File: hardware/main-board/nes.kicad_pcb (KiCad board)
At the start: 2 copper layers, 127 x 114.3 mm, 141 parts, among them J1 Power Jack, J2 Input Board, J3 Speaker, J4 Program, J5 NHD OLED Connector, J6 microSD Socket, Q1 SS8050, Q2 SS8050, Q3 SS8050, SW1 NES Reset, SW2 ESP Reset, U1 R-78E5.0-0.5, U10 74HCT00, U11 PCA9564, U12 MCP7940N, U13 ESP-WROOM-32, U15 EClamp2410P, U2 R-78E3.3-0.5, U3 74LVC1404, U4 RP2A03, U5 74HCT138, U6 LM4889, U7 AS6C6264, U8 MCP40D17, U9 AT28C64B, Y1 21.5 MHz, Y2 32.768 kHz

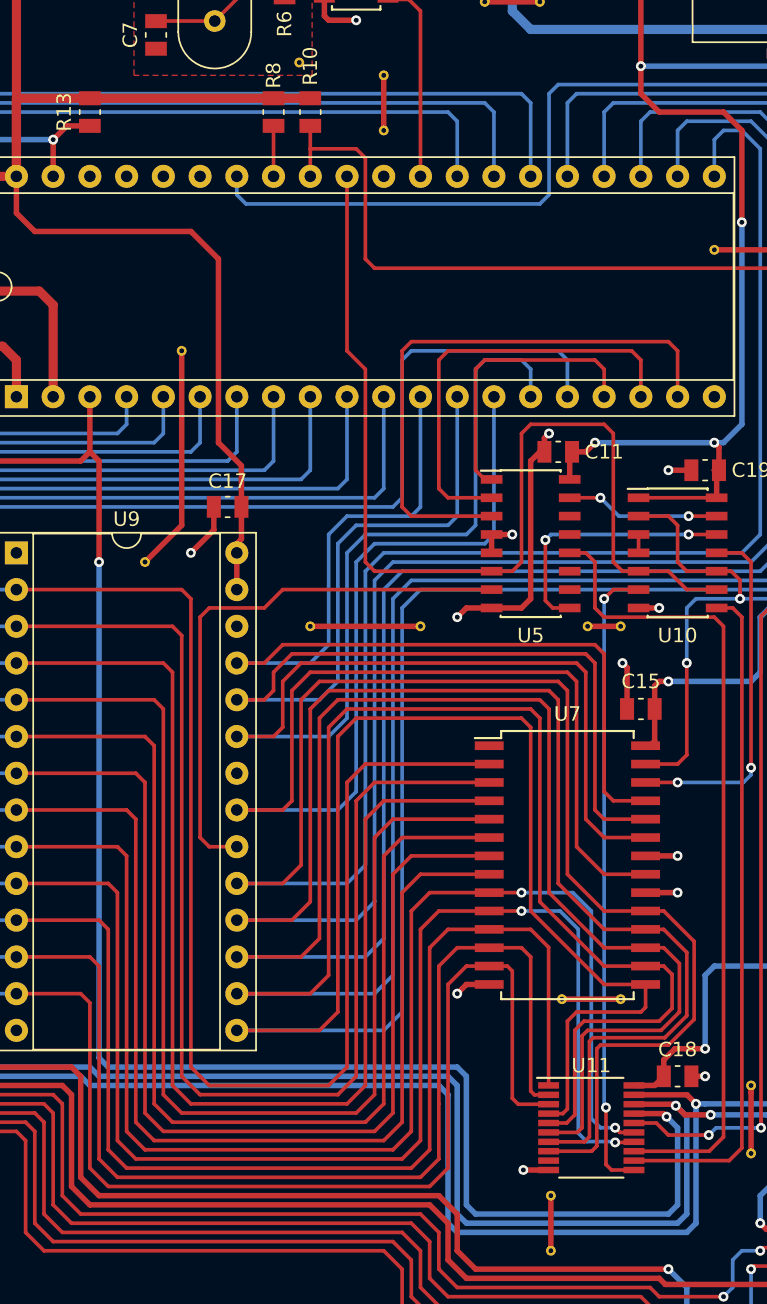
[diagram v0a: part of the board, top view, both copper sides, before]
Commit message: Route the OUT1 line from the RP2A03 to the PCA9564's reset pin
This change gives the NES CPU control over resetting its I2C controller,
for improved error recovery and more predictable startup behavior. Also
added a pull-up resistor, similar to how OUT0 was wired, for a more
predictable "high" voltage.

Fixes #8
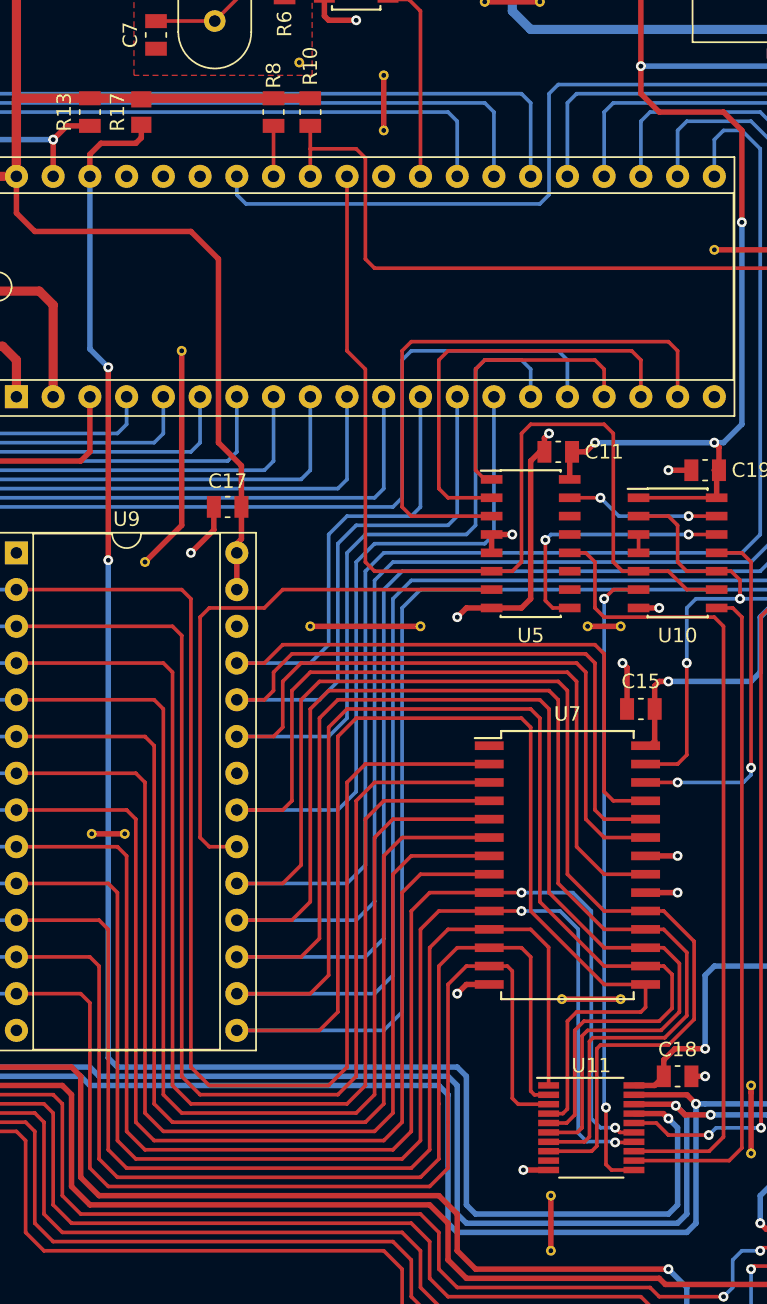
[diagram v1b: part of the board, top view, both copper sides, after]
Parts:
- added R17: 20k, Resistor_SMD:R_0805_2012Metric, F.Cu at (107.7, 49.5)
- added REF**: Via_27mill, lib_fp:Via_27mill, F.Cu at (104.3, 99.4)
- added REF**: Via_27mill, lib_fp:Via_27mill, F.Cu at (106.6, 99.4)
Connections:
- U11 pad 17: /NES CPU/~RST -> /NES CPU/OUT1
- U4 pad 38: Net-(U4-Pad38) -> /NES CPU/OUT1
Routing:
- net /NES CPU/OUT1: track 0.00 -> 126.5 mm, vias 0 -> 3
- net /NES CPU/~RST: track 122.0 -> 21.1 mm, vias 2 -> 0
- net GND: track 409.4 -> 411.7 mm

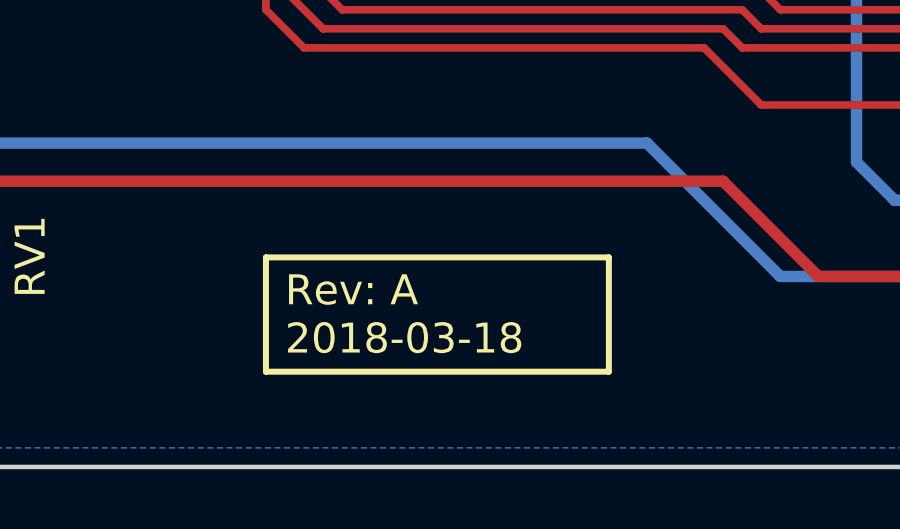
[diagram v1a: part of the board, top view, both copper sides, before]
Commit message: Updated schematic and PCB references for Rev B
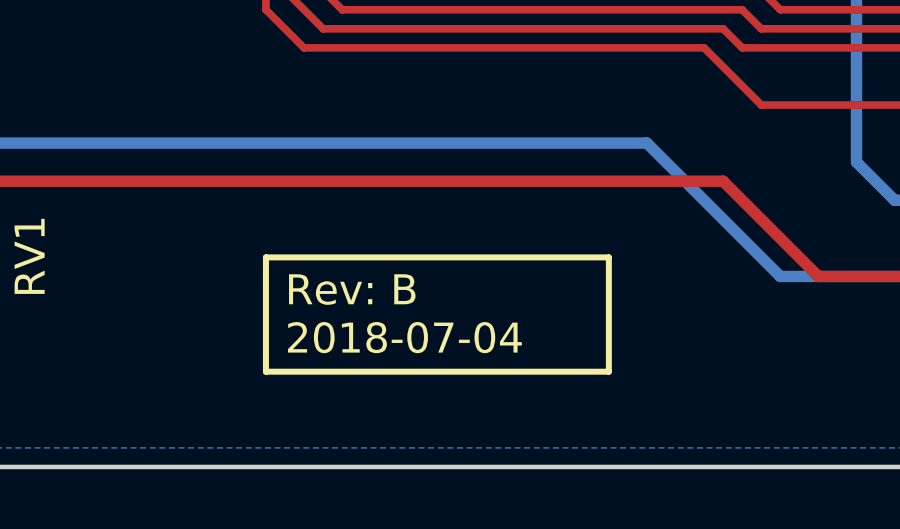
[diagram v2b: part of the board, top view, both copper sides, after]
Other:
- board text added: "Rev: B 2018-07-04"
- board text removed: "Rev: A 2018-03-18"
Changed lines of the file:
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@@
   (title_block
     (title "Nestronic Game Music Synthesizer")
-    (date 2018-03-13)
-    (rev A)
+    (date 2018-07-04)
+    (rev B)
     (company LogicProbe.org)
     (comment 1 "Derek Konigsberg")
@@
   )
   (setup
-    (last_trace_width 0.381)
+    (last_trace_width 0.1524)
     (user_trace_width 0.254)
     (user_trace_width 0.381)
@@
   (gr_line (start 125.73 144.145) (end 137.16 144.145) (angle 90) (layer F.SilkS) (width 0.2))
   (gr_line (start 125.73 140.335) (end 125.73 144.145) (angle 90) (layer F.SilkS) (width 0.2))
-  (gr_text "Rev: A\n2018-03-18" (at 126.365 142.24) (layer F.SilkS)
+  (gr_text "Rev: B\n2018-07-04" (at 126.365 142.24) (layer F.SilkS)
     (effects (font (size 1 1) (thickness 0.15)) (justify left))
   )
